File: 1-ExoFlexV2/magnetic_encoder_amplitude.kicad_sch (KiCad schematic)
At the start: 66 parts, among them J64 5,1k, J65 5,1k, J66 5,1k, J67 5,1k, J68 5,1k, J69 5,1k, U11 SN74LVC1G32DBVR, U12 SN74LVC1G32DBVR

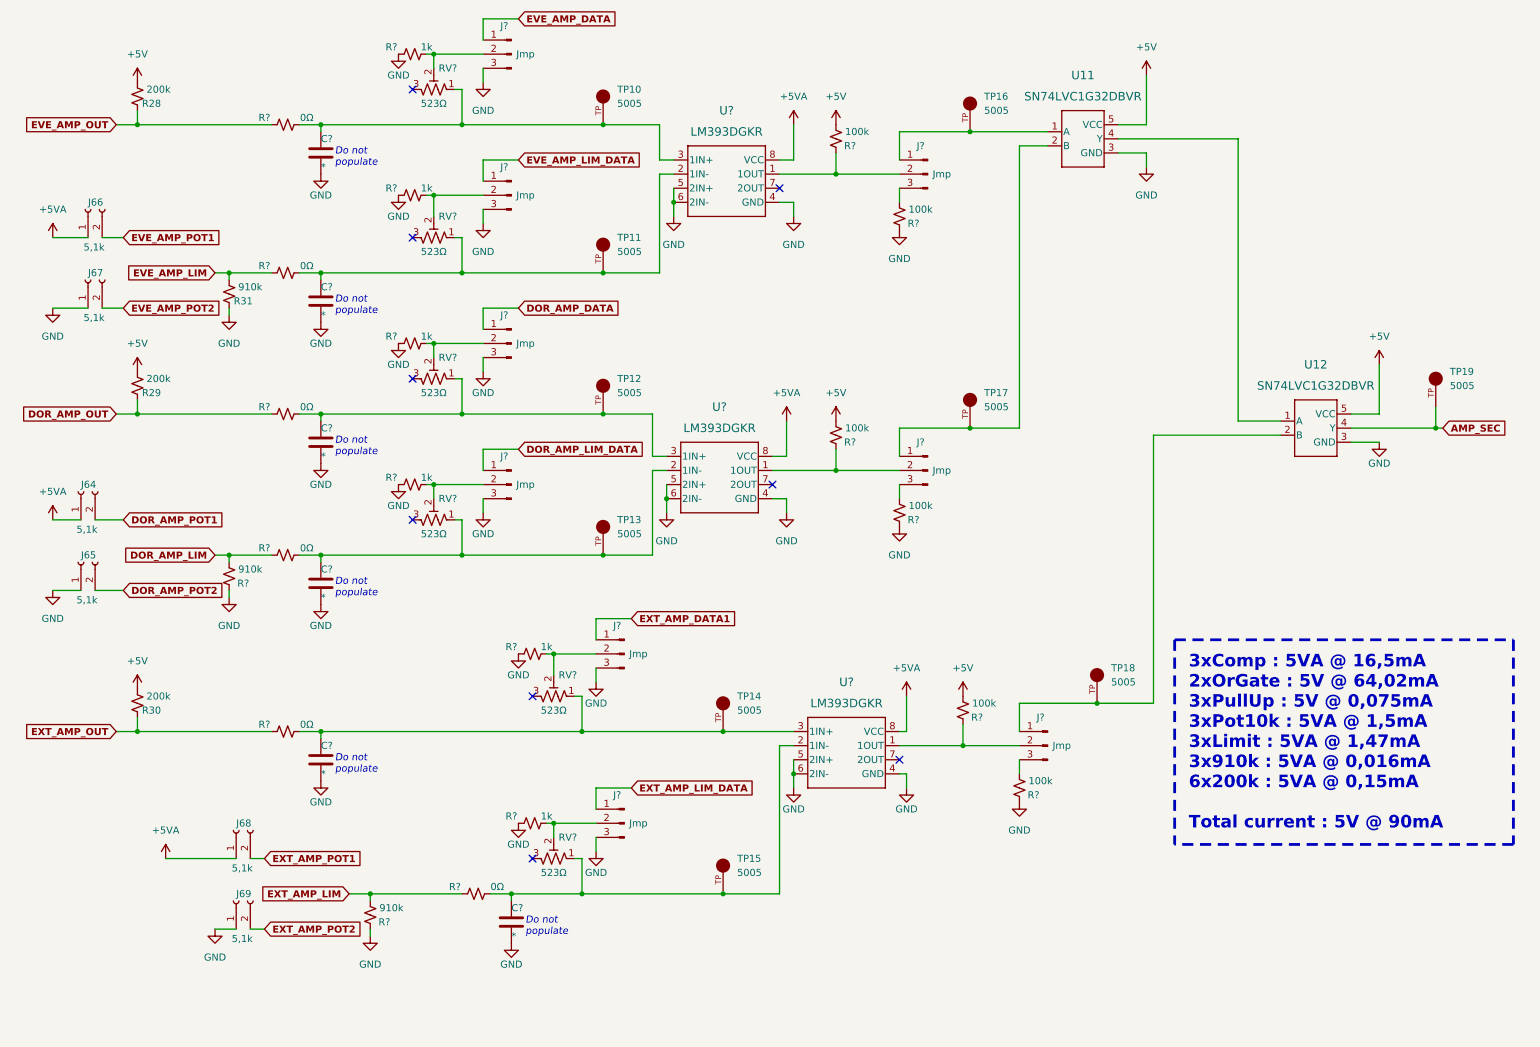
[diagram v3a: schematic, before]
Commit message: Test points et notes
- Ajout de tous les tests point nécessaires
-  Ajoute des sections de notes dans chaque page
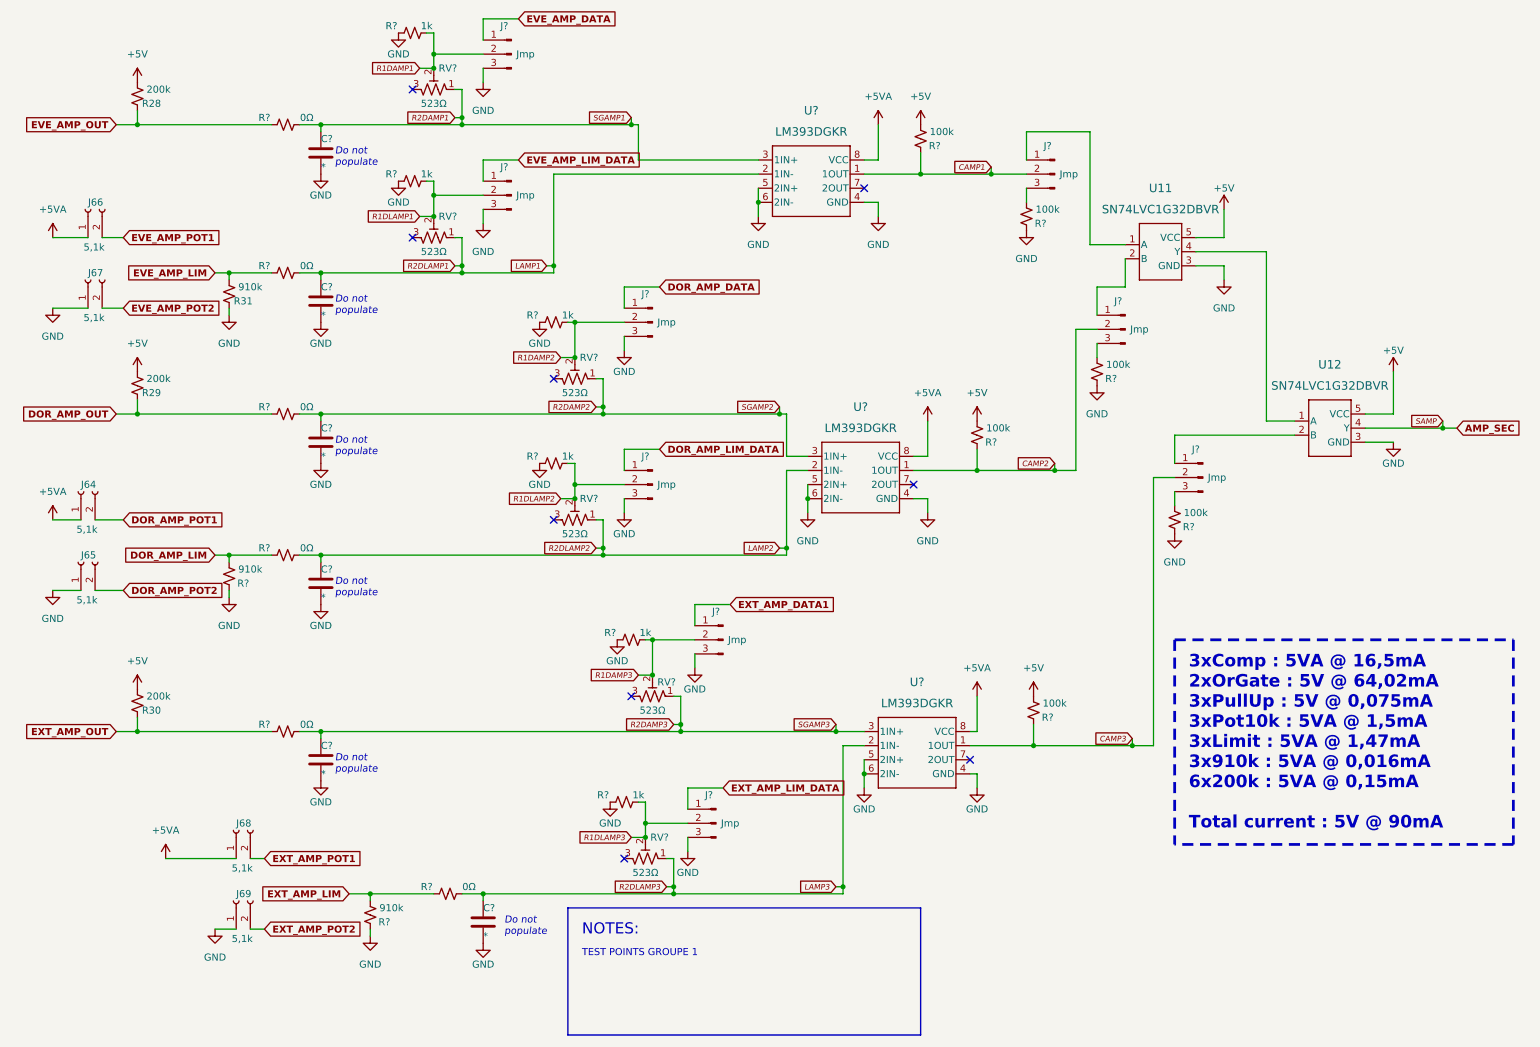
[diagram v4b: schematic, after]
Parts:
- removed TP10, TP11, TP12, TP13, TP14, TP15, TP16, TP17, TP18, TP19: 5005, FootPrint:KEYSTONE_5005, symbol SymLib:5005
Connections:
- net R1DLAMP3: now reaches J?.2 (Pin_2), R?.2, RV?.2
- net R2DAMP3: now reaches C?.1, R?.2, RV?.1, U?.3 (1IN+)
- net R1DAMP3: now reaches J?.2 (Pin_2), R?.2, RV?.2
- net R2DAMP1: now reaches C?.1, R?.2, RV?.1, U?.3 (1IN+)
- net R1DAMP1: now reaches J?.2 (Pin_2), R?.2, RV?.2
- net CAMP3: now reaches J?.2 (Pin_2), R?.2, U?.1 (1OUT)
- net LAMP3: now reaches C?.1, R?.2, RV?.1, U?.2 (1IN-)
- net CAMP1: now reaches J?.2 (Pin_2), R?.2, U?.1 (1OUT)
- net LAMP2: now reaches C?.1, R?.2, RV?.1, U?.2 (1IN-)
- net R1DLAMP2: now reaches J?.2 (Pin_2), R?.2, RV?.2
- net R2DAMP2: now reaches C?.1, R?.2, RV?.1, U?.3 (1IN+)
- net R1DLAMP1: now reaches J?.2 (Pin_2), R?.2, RV?.2
- net R1DAMP2: now reaches J?.2 (Pin_2), R?.2, RV?.2
- net LAMP1: now reaches C?.1, R?.2, RV?.1, U?.2 (1IN-)
- net CAMP2: now reaches J?.2 (Pin_2), R?.2, U?.1 (1OUT)
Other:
- note added: "NOTES:"
- note added: "TEST POINTS GROUPE 1"
- moved on the sheet: C?, J?, R?, RV?, U11, U12, U?

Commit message: Schématisation terminée
- Schéma terminé
- Passage vers le PCB
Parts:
- C16, C17, C18, C19, C20, C21: renamed from C?; value * -> 10nF 10V X5R; footprint Capacitor_SMD:C_0805_2012Metric -> Capacitor_SMD:C_01005_0402Metric; DESCRIPTION (none) -> 10000 pF ±10% 10V Ceramic Capacitor X5R 01005 (0402 Metric); MANUFACTURER (none) -> Murata Electronics; NOTES (none) -> DO NOT POPULATE; PACKAGE (none) -> 01005 (0402 Metric); PART NUMBER (none) -> GRM022R61A103KE19L; TYPE (none) -> SMD
- J59: renamed from J64; value 5,1k -> Tulip Conn; footprint Connector_PinHeader_2.54mm:PinHeader_1x02_P2.54mm_Vertical -> Connector_PinSocket_2.54mm:PinSocket_1x02_P2.54mm_Vertical; DESCRIPTION (none) -> 2 Position Socket Connector 0.100" (2.54mm) Through Hole Go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; MANUFACTURER (none) -> Preci-Dip; PACKAGE (none) -> 2 POS 0.100" (2.54mm); PART NUMBER (none) -> 801-87-002-10-001101; TYPE (none) -> Through Hole
- J60: renamed from J65; value 5,1k -> Tulip Conn; footprint Connector_PinHeader_2.54mm:PinHeader_1x02_P2.54mm_Vertical -> Connector_PinSocket_2.54mm:PinSocket_1x02_P2.54mm_Vertical; DESCRIPTION (none) -> 2 Position Socket Connector 0.100" (2.54mm) Through Hole Go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; MANUFACTURER (none) -> Preci-Dip; PACKAGE (none) -> 2 POS 0.100" (2.54mm); PART NUMBER (none) -> 801-87-002-10-001101; TYPE (none) -> Through Hole
- J61: renamed from J66; value 5,1k -> Tulip Conn; footprint Connector_PinHeader_2.54mm:PinHeader_1x02_P2.54mm_Vertical -> Connector_PinSocket_2.54mm:PinSocket_1x02_P2.54mm_Vertical; DESCRIPTION (none) -> 2 Position Socket Connector 0.100" (2.54mm) Through Hole Go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; MANUFACTURER (none) -> Preci-Dip; PACKAGE (none) -> 2 POS 0.100" (2.54mm); PART NUMBER (none) -> 801-87-002-10-001101; TYPE (none) -> Through Hole
- J62: renamed from J67; value 5,1k -> Tulip Conn; footprint Connector_PinHeader_2.54mm:PinHeader_1x02_P2.54mm_Vertical -> Connector_PinSocket_2.54mm:PinSocket_1x02_P2.54mm_Vertical; DESCRIPTION (none) -> 2 Position Socket Connector 0.100" (2.54mm) Through Hole Go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; MANUFACTURER (none) -> Preci-Dip; PACKAGE (none) -> 2 POS 0.100" (2.54mm); PART NUMBER (none) -> 801-87-002-10-001101; TYPE (none) -> Through Hole
- J63: renamed from J68; value 5,1k -> Tulip Conn; footprint Connector_PinHeader_2.54mm:PinHeader_1x02_P2.54mm_Vertical -> Connector_PinSocket_2.54mm:PinSocket_1x02_P2.54mm_Vertical; DESCRIPTION (none) -> 2 Position Socket Connector 0.100" (2.54mm) Through Hole Go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; MANUFACTURER (none) -> Preci-Dip; PACKAGE (none) -> 2 POS 0.100" (2.54mm); PART NUMBER (none) -> 801-87-002-10-001101; TYPE (none) -> Through Hole
- J64: renamed from J69; value 5,1k -> Tulip Conn; footprint Connector_PinHeader_2.54mm:PinHeader_1x02_P2.54mm_Vertical -> Connector_PinSocket_2.54mm:PinSocket_1x02_P2.54mm_Vertical; DESCRIPTION (none) -> 2 Position Socket Connector 0.100" (2.54mm) Through Hole Go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; MANUFACTURER (none) -> Preci-Dip; PACKAGE (none) -> 2 POS 0.100" (2.54mm); PART NUMBER (none) -> 801-87-002-10-001101; TYPE (none) -> Through Hole
- J65, J66, J67, J68, J69, J70, J71, J72, J73: renamed from J?; value Jmp -> Jumper; footprint (none) -> Connector_PinSocket_2.54mm:PinSocket_1x03_P2.54mm_Vertical; DESCRIPTION (none) -> CONN HEADER VERT 3POS 2.54MM; MANUFACTURER (none) -> Würth Elektronik; PACKAGE (none) -> Square 0.100" (2.54mm); PART NUMBER (none) -> 61300311121; TYPE (none) -> Through Hole
- R35: renamed from R28; value 200k -> 200k 5% 1/8W; DESCRIPTION (none) -> 200 kOhms ±5% 0.125W, 1/8W Chip Resistor 0805 (2012 Metric)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; MANUFACTURER (none) -> Panasonic Electronic Components; PACKAGE (none) -> 0805 (2012 Metric); PART NUMBER (none) -> ERJ-6GEYJ204V; TYPE (none) -> SMD
- R36: renamed from R29; value 200k -> 200k 5% 1/8W; footprint Resistor_SMD:R_0603_1608Metric -> Resistor_SMD:R_0805_2012Metric; DESCRIPTION (none) -> 200 kOhms ±5% 0.125W, 1/8W Chip Resistor 0805 (2012 Metric)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; MANUFACTURER (none) -> Panasonic Electronic Components; PACKAGE (none) -> 0805 (2012 Metric); PART NUMBER (none) -> ERJ-6GEYJ204V; TYPE (none) -> SMD
- R37: renamed from R30; value 200k -> 200k 5% 1/8W; footprint Resistor_SMD:R_0603_1608Metric -> Resistor_SMD:R_0805_2012Metric; DESCRIPTION (none) -> 200 kOhms ±5% 0.125W, 1/8W Chip Resistor 0805 (2012 Metric)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; MANUFACTURER (none) -> Panasonic Electronic Components; PACKAGE (none) -> 0805 (2012 Metric); PART NUMBER (none) -> ERJ-6GEYJ204V; TYPE (none) -> SMD
- R38: renamed from R31; value 910k -> 910k 0,1% 1/8W; DESCRIPTION (none) -> 910 kOhms ±0.1% 0.125W, 1/8W Chip Resistor 0805 (2012 Metri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; MANUFACTURER (none) -> Panasonic Electronic Components; PACKAGE (none) -> 0805 (2012 Metric); PART NUMBER (none) -> ERA-6AEB914V; TYPE (none) -> SMD
- R39, R45: renamed from R?; value 910k -> 910k 0,1% 1/8W; DESCRIPTION (none) -> 910 kOhms ±0.1% 0.125W, 1/8W Chip Resistor 0805 (2012 Metri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; MANUFACTURER (none) -> Panasonic Electronic Components; PACKAGE (none) -> 0805 (2012 Metric); PART NUMBER (none) -> ERA-6AEB914V; TYPE (none) -> SMD
- R40, R41, R42, R43, R44, R48: renamed from R?; DESCRIPTION (none) -> 0 Ohms Jumper Chip Resistor 0805 (2012 Metric) Automotive A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; MANUFACTURER (none) -> Panasonic Electronic Components; PACKAGE (none) -> 0805 (2012 Metric); PART NUMBER (none) -> ERJ-6GEY0R00V; TYPE (none) -> SMD
- R46, R47, R49, R50, R51, R52: renamed from R?; value 1k -> 1k 1% 1/10W; footprint Resistor_SMD:R_0805_2012Metric -> Resistor_SMD:R_0402_1005Metric; DESCRIPTION (none) -> 1 kOhms ±1% 0.1W, 1/10W Chip Resistor 0402 (1005 Metric) Au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; MANUFACTURER (none) -> Panasonic Electronic Components; PACKAGE (none) -> 0402 (1005 Metric); PART NUMBER (none) -> ERJ-2RKF1001X; TYPE (none) -> SMD
- R53, R54, R55, R56, R57, R58: renamed from R?; value 100k -> 100k 5% 1/8W; DESCRIPTION (none) -> 100 kOhms ±5% 0.125W, 1/8W Chip Resistor 0805 (2012 Metric)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; MANUFACTURER (none) -> Panasonic Electronic Components; PACKAGE (none) -> 0805 (2012 Metric); PART NUMBER (none) -> ERJ-6GEYJ104V; TYPE (none) -> SMD
- RV10, RV11, RV12, RV13, RV14, RV9: renamed from RV?; value 523Ω -> Trim 1k; DESCRIPTION (none) -> Trimmer 1k 0,5W PC PIN TOP; MANUFACTURER (none) -> Bourns Inc.; PACKAGE (none) -> Rectangular - 0.275" x 0.260" Face; PART NUMBER (none) -> 3362P-1-102LF; TYPE (none) -> Through Hole
- U20, U21, U22: renamed from U?; value LM393DGKR -> COMP; footprint DGK8 -> FootPrint:DGK8; DESCRIPTION (none) -> Comparator General Purpose Open-Collector, Rail-to-Rail 8-V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; MANUFACTURER (none) -> Texas Instruments; PACKAGE (none) -> 8-TSSOP, 8-MSOP (0.118", 3.00mm Width); PART NUMBER (none) -> LM393DGKR; TYPE (none) -> SMD
- U23: renamed from U11; value SN74LVC1G32DBVR -> OR Gate; DESCRIPTION (none) -> OR Gate IC 1 Channel SOT-23-5; MANUFACTURER (none) -> Texas Instruments; PACKAGE (none) -> SC-74A, SOT-753; PART NUMBER (none) -> SN74LVC1G32DBVR; TYPE (none) -> SMD
- U24: renamed from U12; value SN74LVC1G32DBVR -> OR Gate; DESCRIPTION (none) -> OR Gate IC 1 Channel SOT-23-5; MANUFACTURER (none) -> Texas Instruments; PACKAGE (none) -> SC-74A, SOT-753; PART NUMBER (none) -> SN74LVC1G32DBVR; TYPE (none) -> SMD
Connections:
- net EXT_AMP_DATA1 renamed EXT_AMP_DATA
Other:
- note added: "3xComp : 5VA @ 77,4mA 2xOrGate : 5V @ 64,02mA 3xPullUp : 5V @ 0,075mA 3xPot10k : 5VA @ 30mA 3xLimit : 5VA @ 60mA 3x910k : 5VA @ 0,016mA 6x100k : 5VA @ 0,3mA 6xPot523 : 5VA @ 60mA Total current : 5V @ 69mA 5VA @ 232mA"
- note added: "5,1kΩ"
- note added: "523Ω"
- note removed: "3xComp : 5VA @ 16,5mA 2xOrGate : 5V @ 64,02mA 3xPullUp : 5V @ 0,075mA 3xPot10k : 5VA @ 1,5mA 3xLimit : 5VA @ 1,47mA 3x910k : 5VA @ 0,016mA 6x200k : 5VA @ 0,15mA Total current : 5V @ 90mA"
- moved on the sheet: C16, C19, C20, C21, J70, J71, R40, R51, R55, RV13

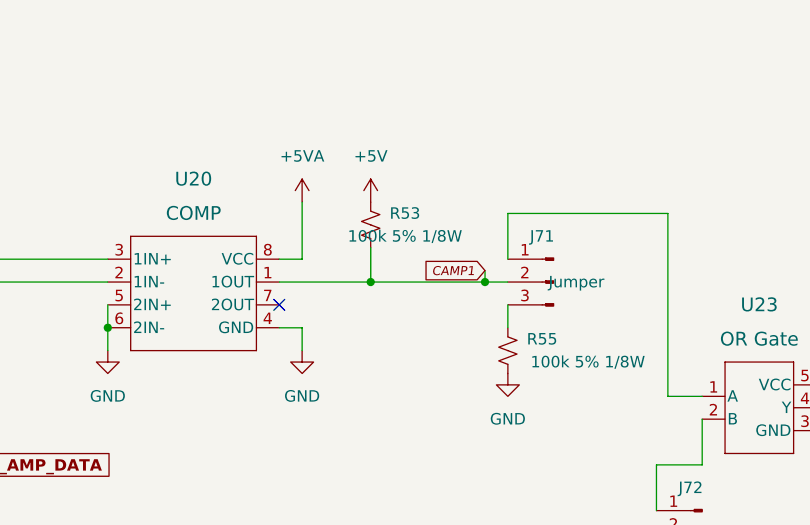
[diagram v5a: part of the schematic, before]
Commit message: Bug NetList
- Ajout de net-tie pour les GND et et les +5V
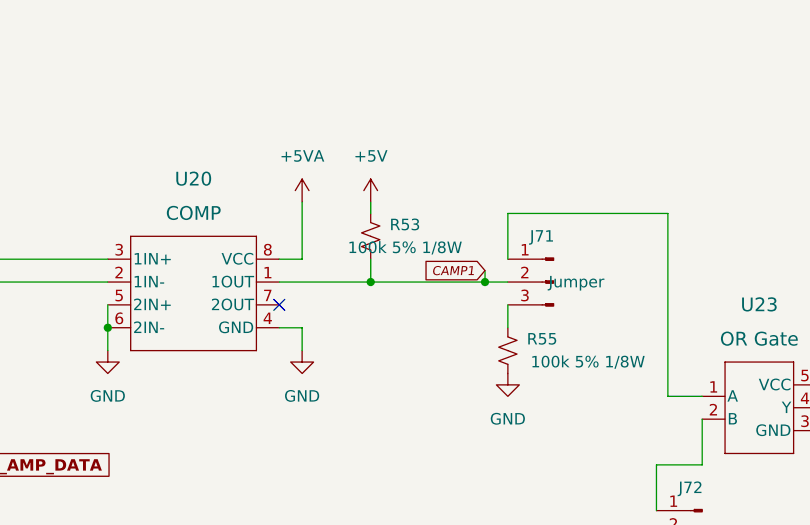
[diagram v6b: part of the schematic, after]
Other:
- moved on the sheet: R53

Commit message: PLACEMENT 1
- Placement des connnecteurs
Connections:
- net +5V: no longer R35.1, R36.1, R37.1
- net +5VA: now also R35.1, R36.1, R37.1
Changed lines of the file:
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@@
-    (pin "1")
-  )
-  (symbol (lib_id "power:+5V") (at 34.29 25.4 0) (unit 1)
-    (in_bom yes) (on_board yes) (fields_autoplaced)
-    (property "Reference" "#PWR0165" (id 0) (at 34.29 29.21 0)
-      (effects (font (size 1.27 1.27)) hide)
-    )
-    (property "Value" "+5V" (id 1) (at 34.29 20.32 0))
-    (property "Footprint" "" (id 2) (at 34.29 25.4 0)
-      (effects (font (size 1.27 1.27)) hide)
-    )
-    (property "Datasheet" "" (id 3) (at 34.29 25.4 0)
-      (effects (font (size 1.27 1.27)) hide)
-    )
     (pin "1")
   )
@@
     (pin "2")
   )
-  (symbol (lib_id "power:+5V") (at 34.29 134.62 0) (unit 1)
-    (in_bom yes) (on_board yes) (fields_autoplaced)
-    (property "Reference" "#PWR0167" (id 0) (at 34.29 138.43 0)
-      (effects (font (size 1.27 1.27)) hide)
-    )
-    (property "Value" "+5V" (id 1) (at 34.29 129.54 0))
-    (property "Footprint" "" (id 2) (at 34.29 134.62 0)
-      (effects (font (size 1.27 1.27)) hide)
-    )
-    (property "Datasheet" "" (id 3) (at 34.29 134.62 0)
-      (effects (font (size 1.27 1.27)) hide)
-    )
-    (pin "1")
-  )
   (symbol (lib_id "power:GND") (at 106.68 93.98 0) (unit 1)
     (in_bom yes) (on_board yes)
@@
     (pin "1")
     (pin "2")
+  )
+  (symbol (lib_id "power:+5VA") (at 34.29 77.47 0) (unit 1)
+    (in_bom yes) (on_board yes) (fields_autoplaced)
+    (property "Reference" "#PWR0166" (id 0) (at 34.29 81.28 0)
+      (effects (font (size 1.27 1.27)) hide)
+    )
+    (property "Value" "+5VA" (id 1) (at 34.29 72.39 0))
+    (property "Footprint" "" (id 2) (at 34.29 77.47 0)
+      (effects (font (size 1.27 1.27)) hide)
+    )
+    (property "Datasheet" "" (id 3) (at 34.29 77.47 0)
+      (effects (font (size 1.27 1.27)) hide)
+    )
+    (pin "1")
   )
   (symbol (lib_id "Device:R_Potentiometer_Trim_US") (at 87.63 53.34 270) (mirror x) (unit 1)
@@
     (pin "1")
   )
+  (symbol (lib_id "power:+5VA") (at 34.29 25.4 0) (unit 1)
+    (in_bom yes) (on_board yes) (fields_autoplaced)
+    (property "Reference" "#PWR0165" (id 0) (at 34.29 29.21 0)
+      (effects (font (size 1.27 1.27)) hide)
+    )
+    (property "Value" "+5VA" (id 1) (at 34.29 20.32 0))
+    (property "Footprint" "" (id 2) (at 34.29 25.4 0)
+      (effects (font (size 1.27 1.27)) hide)
+    )
+    (property "Datasheet" "" (id 3) (at 34.29 25.4 0)
+      (effects (font (size 1.27 1.27)) hide)
+    )
+    (pin "1")
+  )
   (symbol (lib_id "power:GND") (at 81.28 43.18 0) (unit 1)
     (in_bom yes) (on_board yes)
@@
     (pin "1")
   )
-  (symbol (lib_id "power:+5V") (at 34.29 77.47 0) (unit 1)
-    (in_bom yes) (on_board yes) (fields_autoplaced)
-    (property "Reference" "#PWR0166" (id 0) (at 34.29 81.28 0)
-      (effects (font (size 1.27 1.27)) hide)
-    )
-    (property "Value" "+5V" (id 1) (at 34.29 72.39 0))
-    (property "Footprint" "" (id 2) (at 34.29 77.47 0)
-      (effects (font (size 1.27 1.27)) hide)
-    )
-    (property "Datasheet" "" (id 3) (at 34.29 77.47 0)
-      (effects (font (size 1.27 1.27)) hide)
-    )
-    (pin "1")
-  )
   (symbol (lib_id "power:GND") (at 185.42 152.4 0) (unit 1)
     (in_bom yes) (on_board yes)
@@
     (pin "2")
   )
+  (symbol (lib_id "power:+5VA") (at 34.29 134.62 0) (unit 1)
+    (in_bom yes) (on_board yes) (fields_autoplaced)
+    (property "Reference" "#PWR0167" (id 0) (at 34.29 138.43 0)
+      (effects (font (size 1.27 1.27)) hide)
+    )
+    (property "Value" "+5VA" (id 1) (at 34.29 129.54 0))
+    (property "Footprint" "" (id 2) (at 34.29 134.62 0)
+      (effects (font (size 1.27 1.27)) hide)
+    )
+    (property "Datasheet" "" (id 3) (at 34.29 134.62 0)
+      (effects (font (size 1.27 1.27)) hide)
+    )
+    (pin "1")
+  )
   (symbol (lib_id "power:GND") (at 97.79 180.34 0) (unit 1)
